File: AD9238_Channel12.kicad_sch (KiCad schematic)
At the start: 55 parts, among them J2 BWSMA-KE-P001, J3 BWSMA-KE-P001, U10 AD8065, U11 AD8138, U12 AD8138, U13 AD9238, U9 AD8065

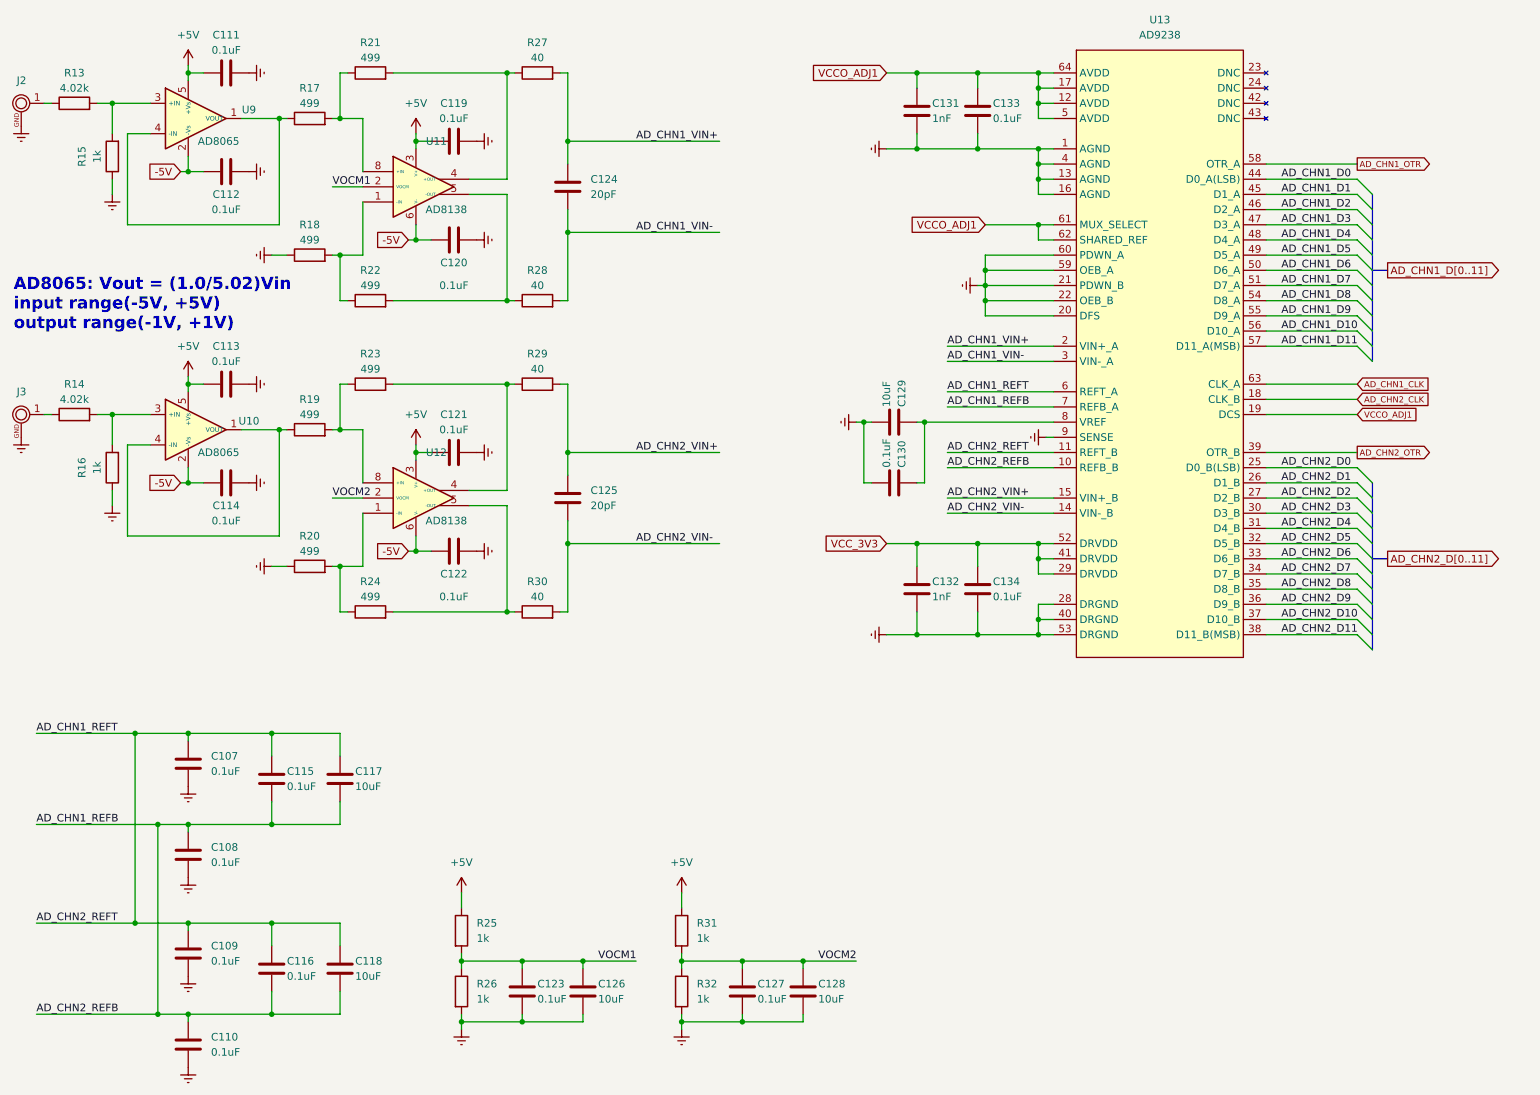
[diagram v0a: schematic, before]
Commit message: 变压器输入+两块DDR3
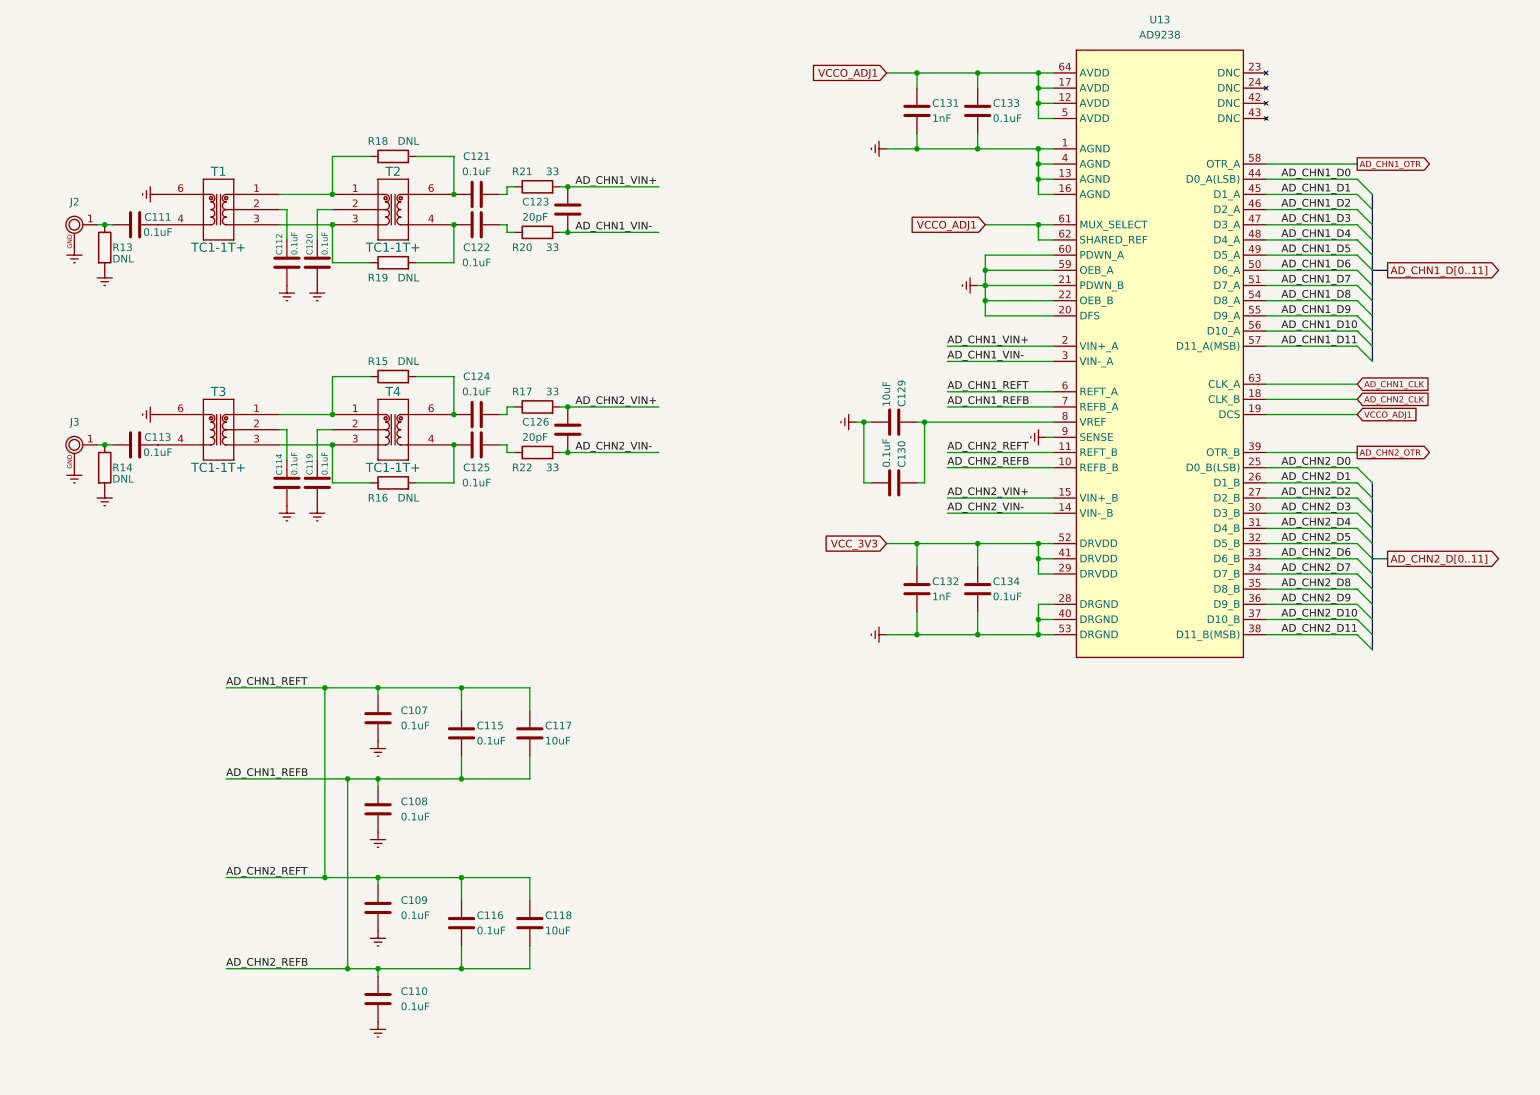
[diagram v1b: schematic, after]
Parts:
- removed C127: 0.1uF, Capacitor_SMD:C_0402_1005Metric, symbol Device:C
- removed C128: 10uF, Capacitor_SMD:C_0603_1608Metric, symbol Device:C
- removed R23, R24: 499, Resistor_SMD:R_0402_1005Metric, symbol Device:R
- removed R25, R26, R31, R32: 1k, Resistor_SMD:R_0402_1005Metric, symbol Device:R
- removed R27, R28, R29, R30: 40, Resistor_SMD:R_0402_1005Metric, symbol Device:R
- removed U10, U9: AD8065, Package_TO_SOT_SMD:SOT-23-5, symbol Zynq7020_AD9238:AD8065
- removed U11, U12: AD8138, Package_SO:SOIC-8_3.9x4.9mm_P1.27mm, symbol Zynq7020_AD9238:AD8138
- added T1, T2, T3, T4: TC1-1T+, Transformer_SMD:Transformer_MiniCircuits_AT224-1A, symbol Zynq7020_AD9238:TC1-1T+
- C123: value 0.1uF -> 20pF; footprint Capacitor_SMD:C_0402_1005Metric -> Capacitor_SMD:C_01005_0402Metric
- C124, C125: value 20pF -> 0.1uF; footprint Capacitor_SMD:C_01005_0402Metric -> Capacitor_SMD:C_0402_1005Metric
- C126: value 10uF -> 20pF; footprint Capacitor_SMD:C_0603_1608Metric -> Capacitor_SMD:C_01005_0402Metric
- R13, R14: value 4.02k -> DNL
- R15, R16: value 1k -> DNL
- R17, R20, R21, R22: value 499 -> 33
- R18, R19: value 499 -> DNL
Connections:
- net AD_CHN1_VIN+: now also C123.1, R21.2; no longer C124.2
- net AD_CHN1_VIN-: now also C123.2, R20.2; no longer C124.1
- net AD_CHN2_VIN+: now also C126.1, R17.2; no longer C125.2
- net AD_CHN2_VIN-: now also C126.2, R22.2; no longer C125.1
- net Earth: now also C112.1, C114.1, C119.1, C120.1, R13.2, R14.2, T1.6, T3.6; no longer C111.2, C112.2, C113.2, C114.2, C119.2, C120.2, C121.2, C122.2, C123.2, C126.2, R15.1, R16.1, R18.1, R20.1
- net at J2.1 (IN), R13.1: now also C111.1
- net at R22.1: now also C125.2; no longer R18.2
- net at R21.1: now also C121.2; no longer R17.2
- net at R17.1: now also C124.2
- net at R19.2: now also C122.1, T2.4
- net at J3.1 (IN), R14.1: now also C113.1
- net at R19.1: now also T1.3, T2.3
- net at R16.2: now also C125.1, T4.4; no longer R14.2
- net at R15.2: now also C124.1, T4.6; no longer R13.2
- removed net +5V: C111.1, C113.1, C119.1, C121.1
- removed net -5V: C112.1, C114.1, C120.1, C122.1
- removed net VOCM1: C123.1, C126.1
- new net: C111.2, T1.4
- new net: C114.2, T3.2
- new net: C113.2, T3.4
- new net: R15.1, T3.1, T4.1
- new net: R16.1, T3.3, T4.3
- new net: R18.1, T1.1, T2.1
- new net: C112.2, T1.2
- new net: C121.1, R18.2, T2.6
- new net: C120.2, T2.2
- new net: C122.2, R20.1
- new net: C119.2, T4.2
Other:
- note removed: "AD8065: Vout = (1.0/5.02)Vin input range(-5V, +5V) output range(-1V, +1V)"
- moved on the sheet: C107, C108, C109, C110, C115, C116, C117, C118

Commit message: 删除-5V电源，添加eMMC模块接口
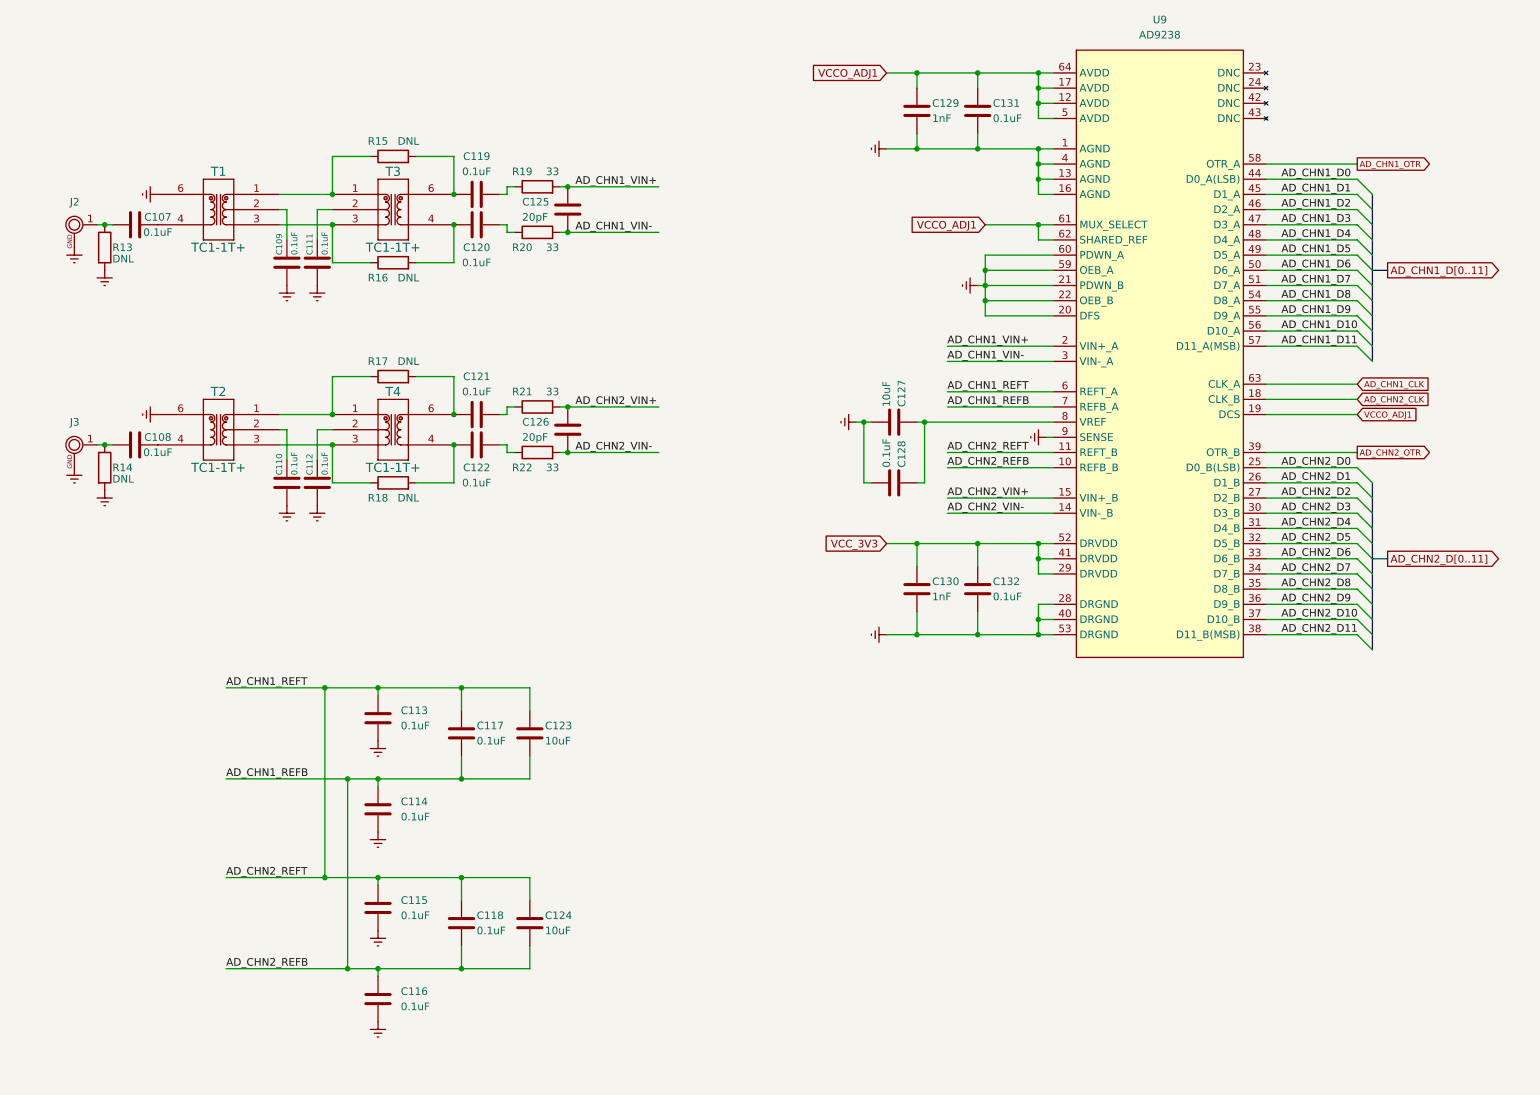
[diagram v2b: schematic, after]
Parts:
- renumbered C111 to C107, C113 to C108, C112 to C109, C114 to C110, C120 to C111, C119 to C112, C107 to C113, C108 to C114, C109 to C115, C110 to C116, C115 to C117, C116 to C118, C121 to C119, C122 to C120, C124 to C121, C125 to C122, C117 to C123, C118 to C124, C123 to C125, C129 to C127, C130 to C128, C131 to C129, C132 to C130, C133 to C131, C134 to C132, R18 to R15, R19 to R16, R15 to R17, R16 to R18, R21 to R19, R17 to R21, T3 to T2, T2 to T3, U13 to U9
